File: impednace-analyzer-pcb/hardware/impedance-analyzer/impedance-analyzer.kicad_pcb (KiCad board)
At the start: 2 copper layers, 61.9 x 56.5 mm, 17 parts, among them J1 AD9833, J10 Conn_01x08, J11 Conn_01x08, J12 Conn_01x08, J2 ADS1256_SPI, J3 ADS1256_AIN, J4 UNO_POWER, J5 UNO_ANALOG, J6 UNO_DIGITAL_LOW, J7 UNO_DIGITAL_HIGH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

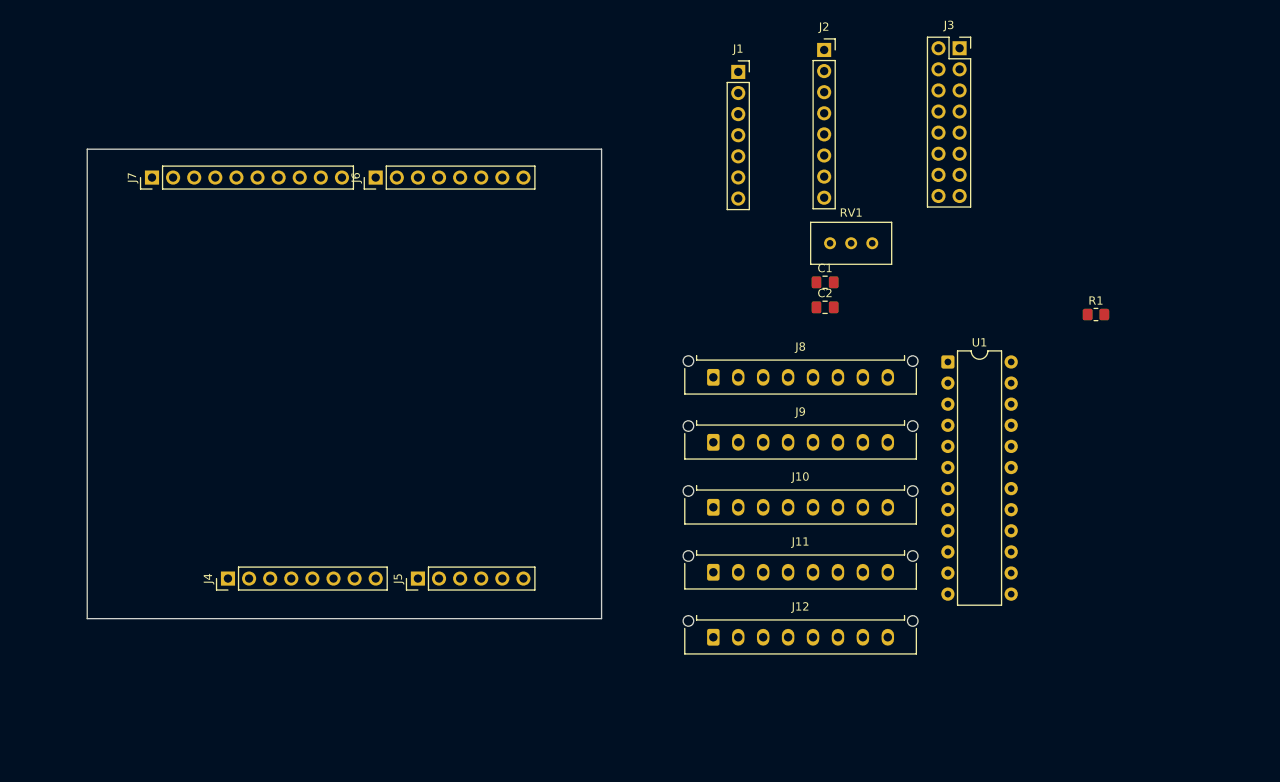
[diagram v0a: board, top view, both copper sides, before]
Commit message: finished placement and started routing
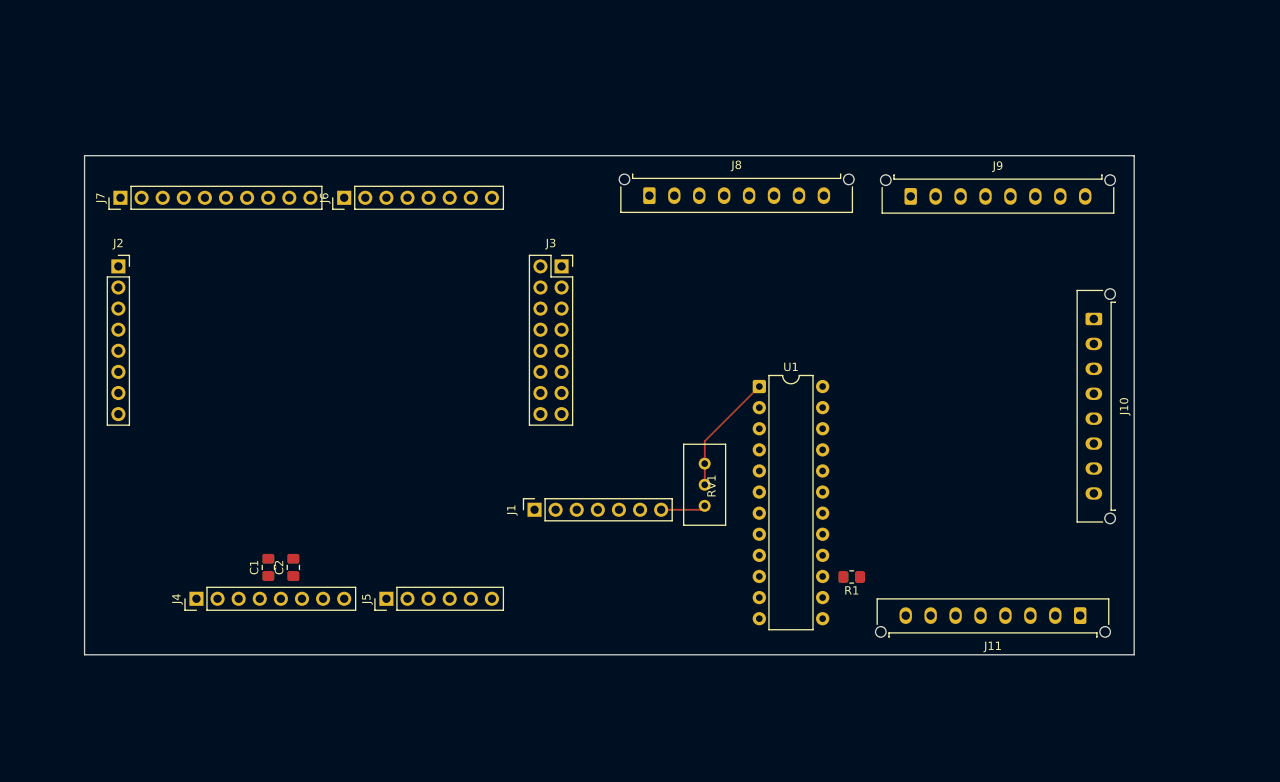
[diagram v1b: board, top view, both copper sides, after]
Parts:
- removed J12: Conn_01x08, Connector_Molex:Molex_Micro-Fit_3.0_43650-0815_1x08_P3.00mm_Vertical
- moved J2 88.8 mm to (125.7, 86.3)
- moved C1 75.3 mm to (143.8, 122.5), turned to 90 degrees
- moved C2 71.2 mm to (146.8, 122.5), turned to 90 degrees
- moved J1 58.1 mm to (175.8, 115.5), turned to 90 degrees
- moved J3 54.6 mm to (179.1, 86.3)
- moved J10 51.1 mm to (243.1, 92.6), turned to -90 degrees
- moved J11 44.5 mm to (241.5, 128.3), turned to 180 degrees
- moved R1 43.1 mm to (214.0, 123.6), turned to 180 degrees
- moved J9 38.0 mm to (221.1, 77.8)
- moved RV1 37.5 mm to (196.3, 115.1), turned to -90 degrees
- moved J8 23.2 mm to (189.7, 77.7)
- moved U1 22.9 mm to (202.9, 100.7)
- moved J5 4.51 mm to (158.0, 126.3)
- moved J7 4.51 mm to (126.0, 78.0)
- moved J4 4.51 mm to (135.1, 126.3)
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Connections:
- J3 pad 1: GND -> AD9833_OUT
- J3 pad 2: AD9833_OUT -> GND
- J3 pad 3: GND -> VMID_NODE
- J3 pad 4: VMID_NODE -> GND
- U1 pad 20: unconnected-(U1-I11-Pad20) -> JACK3_SIG
- U1 pad 21: unconnected-(U1-I10-Pad21) -> JACK2_SIG
- U1 pad 22: unconnected-(U1-I9-Pad22) -> JACK1_SIG
- U1 pad 23: unconnected-(U1-I8-Pad23) -> JACK0_SIG
- U1 pad 5: JACK4_SIG -> unconnected-(U1-I4-Pad5)
- U1 pad 6: JACK3_SIG -> unconnected-(U1-I3-Pad6)
- U1 pad 7: JACK2_SIG -> unconnected-(U1-I2-Pad7)
- U1 pad 8: JACK1_SIG -> unconnected-(U1-I1-Pad8)
- U1 pad 9: JACK0_SIG -> unconnected-(U1-I0-Pad9)
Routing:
- net VMID_NODE: track 0.00 -> 14.5 mm
- net AD9833_OUT: track 0.00 -> 5.43 mm
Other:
- board size 61.9 x 56.5 mm -> 126.3 x 60.1 mm

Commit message: finished routing, waiting review
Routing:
- net +5V: track 0.00 -> 292.0 mm, vias 0 -> 12
- net DB_S1: track 0.00 -> 205.0 mm, vias 0 -> 6
- net DB_S2: track 0.00 -> 197.7 mm, vias 0 -> 6
- net DB_S3: track 0.00 -> 169.2 mm, vias 0 -> 8
- net DB_EN: track 0.00 -> 157.7 mm, vias 0 -> 6
- net DB_S0: track 0.00 -> 148.8 mm
- net SCLK: track 0.00 -> 81.7 mm, vias 0 -> 2
- net MB_S2: track 0.00 -> 81.6 mm, vias 0 -> 2
- net MB_S1: track 0.00 -> 81.1 mm
- net MB_S3: track 0.00 -> 80.8 mm
- net SDATA: track 0.00 -> 80.7 mm, vias 0 -> 3
- net MB_S0: track 0.00 -> 79.9 mm
- net FSYNC: track 0.00 -> 78.6 mm
- net MB_EN: track 0.00 -> 77.4 mm
- net JACK3_SIG: track 0.00 -> 56.7 mm
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- added copper zone on B.Cu, net GND
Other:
- board size 126.3 x 60.1 mm -> 127.1 x 61.8 mm
